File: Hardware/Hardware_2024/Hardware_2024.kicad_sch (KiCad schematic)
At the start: 53 parts, among them U1 Raspberry_Pi, U2 SHHD003A0A, U3 MCP3008

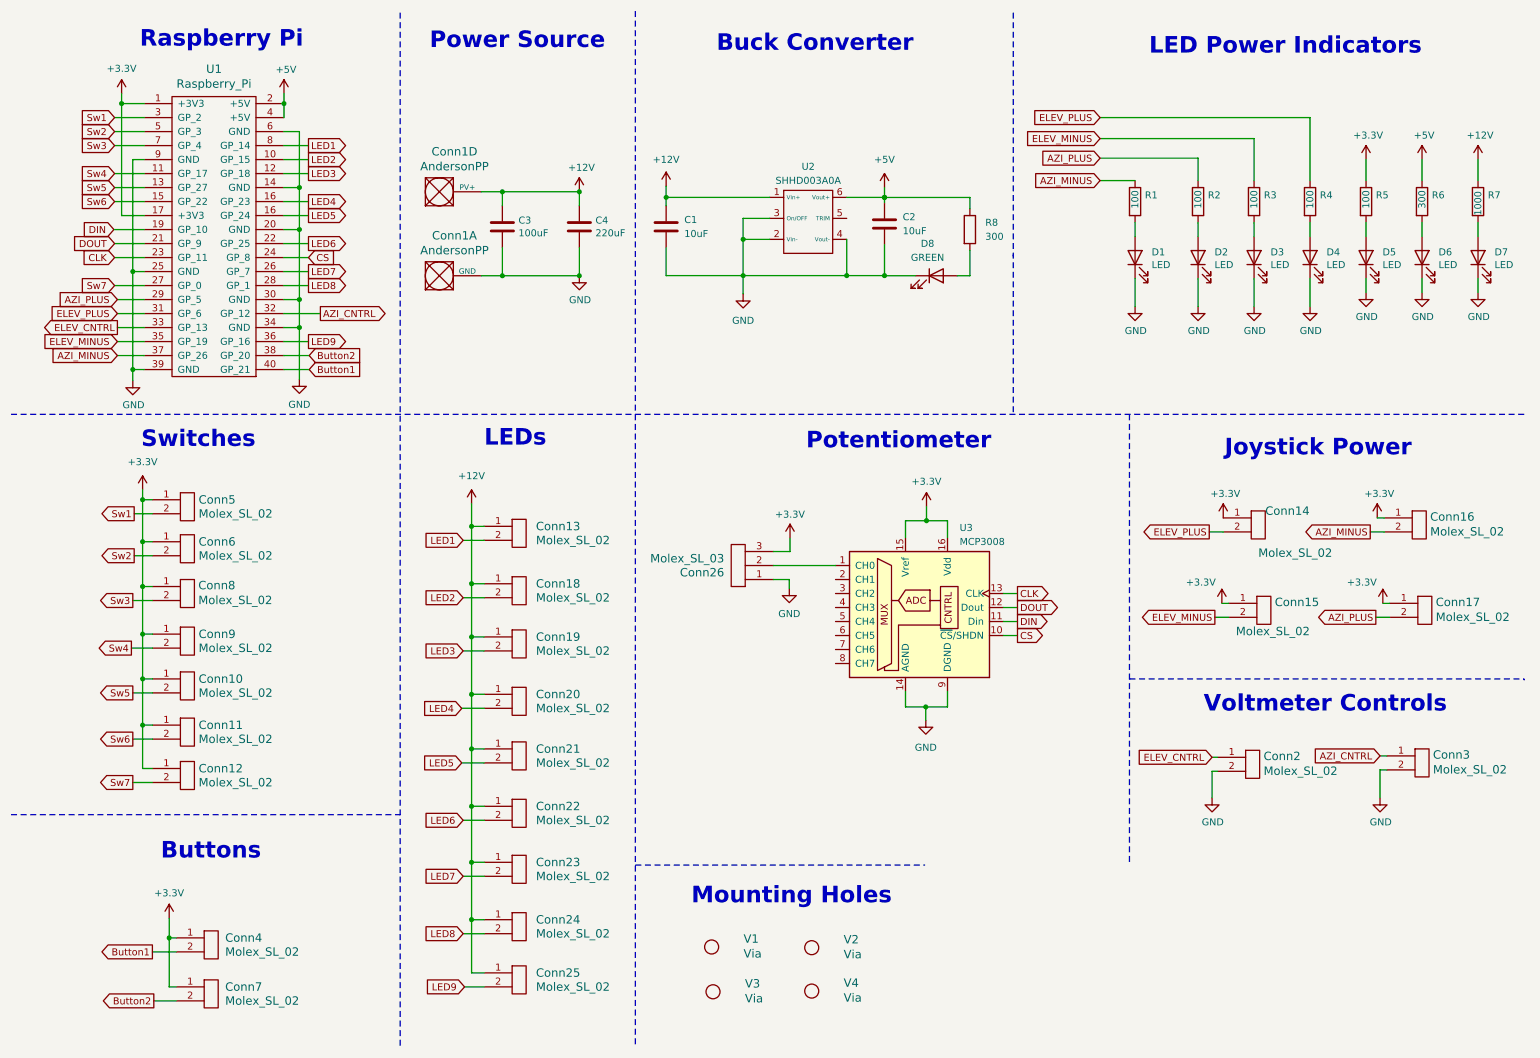
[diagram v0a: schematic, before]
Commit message: assigned footprints worked on layout
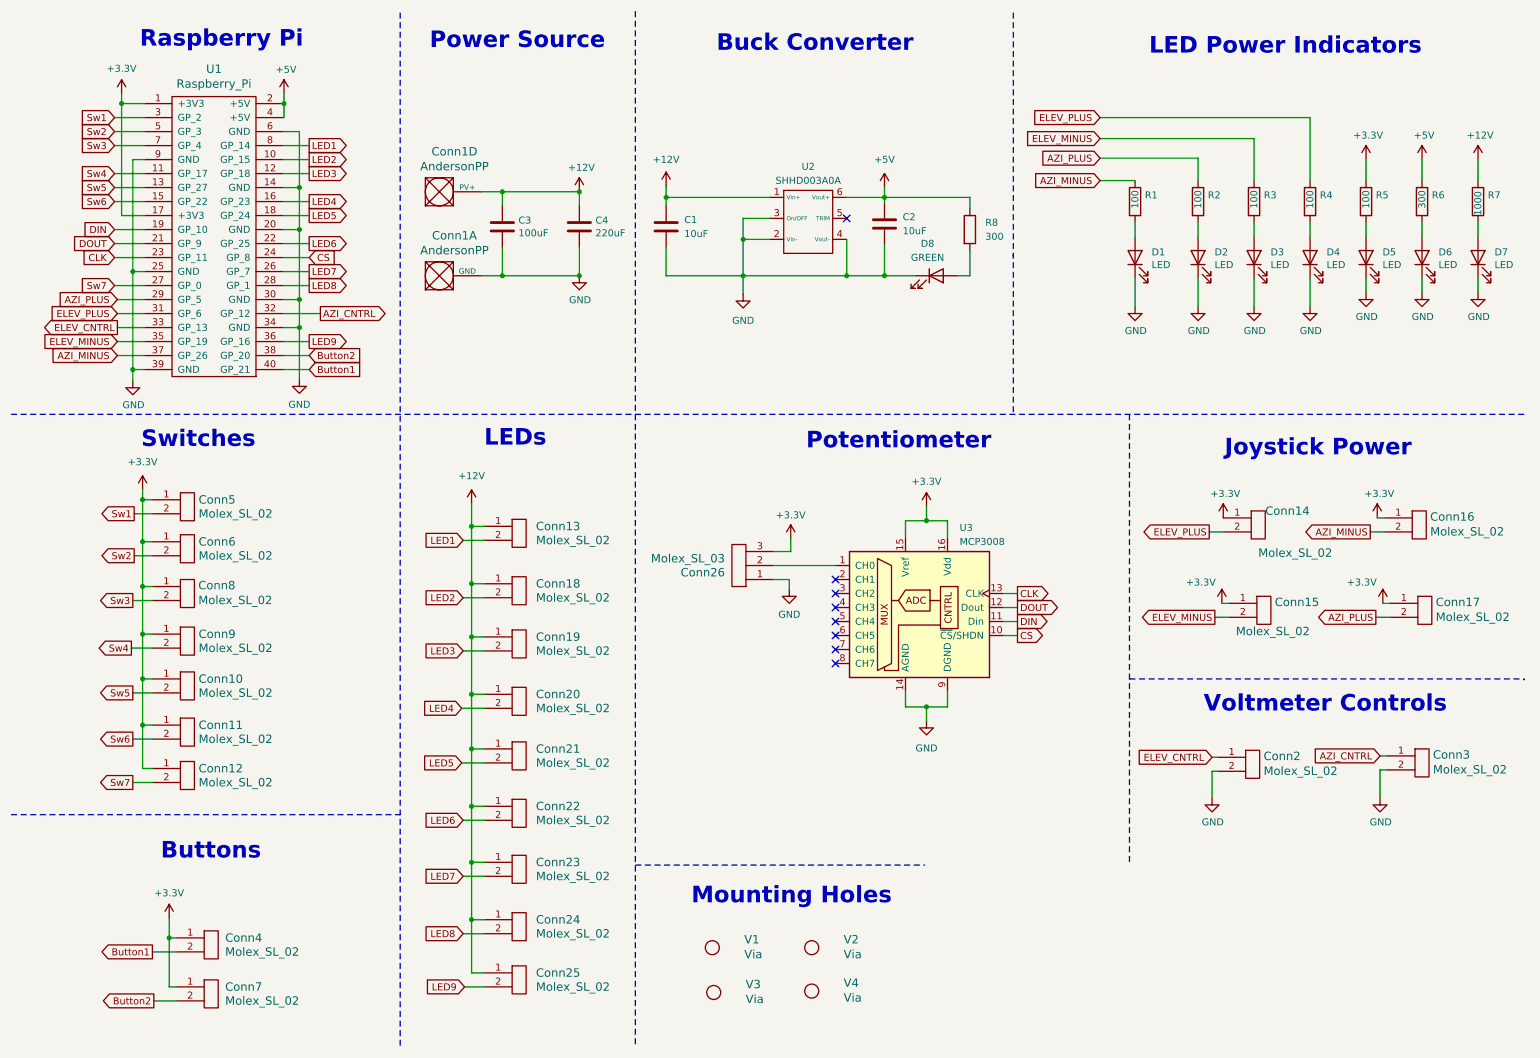
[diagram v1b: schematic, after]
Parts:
- C1, C2: footprint (none) -> Capacitor_SMD:C_0603_1608Metric
- Conn10, Conn11, Conn12, Conn13, Conn18, Conn19, Conn20, Conn21, Conn22, Conn23, Conn24, Conn25, Conn4, Conn5, Conn6, Conn7, Conn9: footprint (none) -> MRDT_Connectors:MOLEX_SL_02_Vertical
- Conn14, Conn16, Conn2, Conn3: footprint MRDT_Connectors:MOLEX_SL_02_Horizontal -> MRDT_Connectors:MOLEX_SL_02_Vertical
- Conn26: footprint (none) -> MRDT_Connectors:MOLEX_SL_03_Horizontal
- D8: footprint (none) -> LED_SMD:LED_0603_1608Metric_Pad1.05x0.95mm_HandSolder
- R8: footprint (none) -> Resistor_SMD:R_0603_1608Metric_Pad0.98x0.95mm_HandSolder
- U2: footprint MRDT_Devices:SHHD003A0A-SRZ -> SHHD003A04A41:SHHD003A0A-SRZ
- U3: footprint (none) -> Package_DIP:DIP-16_W7.62mm
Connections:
- net LED5: now also U1.18 (GP_24); no longer U1.16 (GP_24)
- no-connect marks 0 -> 8

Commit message: finished organizing. traces need work
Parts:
- removed D8: GREEN, LED_SMD:LED_0603_1608Metric_Pad1.05x0.95mm_HandSolder, symbol Device:LED
- removed R8: 300, Resistor_SMD:R_0603_1608Metric_Pad0.98x0.95mm_HandSolder, symbol Device:R
- Conn26: footprint MRDT_Connectors:MOLEX_SL_03_Horizontal -> MRDT_Connectors:MOLEX_SL_03_Vertical
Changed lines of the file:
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@@
   (junction (at 39.878 179.324) (diameter 0) (color 0 0 0 0)
-  )
-  (junction (at 169.672 59.182) (diameter 0) (color 0 0 0 0)
   )
   (junction (at 100.33 43.942) (diameter 0) (color 0 0 0 0)
@@
     (stroke (width 0) (type default))
   )
-  (wire (pts (xy 185.166 44.958) (xy 169.672 44.958))
-    (stroke (width 0) (type default))
-  )
   (wire (pts (xy 94.742 155.448) (xy 94.742 145.034))
     (stroke (width 0) (type default))
@@
     (stroke (width 0) (type default))
   )
-  (wire (pts (xy 185.166 54.61) (xy 185.166 59.182))
-    (stroke (width 0) (type default))
-  )
   (wire (pts (xy 94.742 135.128) (xy 97.028 135.128))
     (stroke (width 0) (type default))
@@
     (stroke (width 0) (type default))
   )
-  (wire (pts (xy 185.166 46.99) (xy 185.166 44.958))
-    (stroke (width 0) (type default))
-  )
   (wire (pts (xy 93.218 117.602) (xy 97.028 117.602))
     (stroke (width 0) (type default))
@@
     (stroke (width 0) (type default))
   )
-  (wire (pts (xy 175.26 59.182) (xy 169.672 59.182))
-    (stroke (width 0) (type default))
-  )
   (wire (pts (xy 60.706 40.64) (xy 65.278 40.64))
     (stroke (width 0) (type default))
@@
   (polyline (pts (xy 193.04 55.626) (xy 193.04 55.372))
     (stroke (width 0) (type dash))
-  )
-  (wire (pts (xy 185.166 59.182) (xy 182.88 59.182))
-    (stroke (width 0) (type default))
   )
   (wire (pts (xy 226.568 64.77) (xy 226.568 59.69))
@@
     )
     (property "Value" "10uF" (at 172.974 51.054 0)
-      (effects (font (size 1.27 1.27)) (justify left))
+      (effects (font (size 1.27 1.27)) (justify left) hide)
     )
     (property "Footprint" "Capacitor_SMD:C_0603_1608Metric" (at 170.6372 53.594 0)
@@
     )
   )
-  (symbol (lib_id "Device:R") (at 185.166 50.8 0) (unit 1)
-    (in_bom yes) (on_board yes) (dnp no) (fields_autoplaced)
-    (property "Reference" "R8" (at 187.96 49.53 0)
-      (effects (font (size 1.27 1.27)) (justify left))
-    )
-    (property "Value" "300" (at 187.96 52.07 0)
-      (effects (font (size 1.27 1.27)) (justify left))
-    )
-    (property "Footprint" "Resistor_SMD:R_0603_1608Metric_Pad0.98x0.95mm_HandSolder" (at 183.388 50.8 90)
-      (effects (font (size 1.27 1.27)) hide)
-    )
-    (property "Datasheet" "~" (at 185.166 50.8 0)
-      (effects (font (size 1.27 1.27)) hide)
-    )
-    (pin "1")
-    (pin "2")
-    (instances
-      (project "Hardware_2024"
-        (path "/925b1423-756e-4600-b210-badb8d52bba3"
-          (reference "R8") (unit 1)
-        )
-      )
-    )
-  )
   (symbol (lib_id "power:+3.3V") (at 152.654 106.934 0) (unit 1)
     (in_bom yes) (on_board yes) (dnp no)
@@
         (path "/925b1423-756e-4600-b210-badb8d52bba3"
           (reference "#PWR013") (unit 1)
-        )
-      )
-    )
-  )
-  (symbol (lib_id "Device:LED") (at 179.07 59.182 0) (unit 1)
-    (in_bom yes) (on_board yes) (dnp no) (fields_autoplaced)
-    (property "Reference" "D8" (at 177.4825 53.34 0)
-      (effects (font (size 1.27 1.27)))
-    )
-    (property "Value" "GREEN" (at 177.4825 55.88 0)
-      (effects (font (size 1.27 1.27)))
-    )
-    (property "Footprint" "LED_SMD:LED_0603_1608Metric_Pad1.05x0.95mm_HandSolder" (at 179.07 59.182 0)
-      (effects (font (size 1.27 1.27)) hide)
-    )
-    (property "Datasheet" "~" (at 179.07 59.182 0)
-      (effects (font (size 1.27 1.27)) hide)
-    )
-    (pin "1")
-    (pin "2")
-    (instances
-      (project "Hardware_2024"
-        (path "/925b1423-756e-4600-b210-badb8d52bba3"
-          (reference "D8") (unit 1)
         )
       )
@@
       (effects (font (size 1.524 1.524)) (justify left))
     )
-    (property "Footprint" "MRDT_Connectors:MOLEX_SL_03_Horizontal" (at 144.526 107.95 0)
-      (effects (font (size 1.524 1.524)) hide)
-    )
+    (property "Footprint" "MRDT_Connectors:MOLEX_SL_03_Vertical" (at 144.526 107.95 0)
+      (effects (font (size 1.524 1.524)) hide)
+    )

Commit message: Updated with changes
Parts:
- removed C3: 100uF, Capacitor_THT:CP_Radial_D6.3mm_P2.50mm, symbol Device:C
- removed C4: 220uF, Capacitor_THT:CP_Radial_D6.3mm_P2.50mm, symbol Device:C
- removed Conn10, Conn11, Conn12, Conn13, Conn18, Conn19, Conn20, Conn21, Conn22, Conn23, Conn24, Conn25, Conn4, Conn5, Conn6, Conn7, Conn8, Conn9: Molex_SL_02, MRDT_Connectors:MOLEX_SL_02_Vertical, symbol MRDT_Connectors:Molex_SL_02
- removed Conn26: Molex_SL_03, MRDT_Connectors:MOLEX_SL_03_Vertical, symbol MRDT_Connectors:Molex_SL_03
- removed D1, D2, D3, D4: LED, LED_SMD:LED_0603_1608Metric_Pad1.05x0.95mm_HandSolder, symbol Device:LED
- removed R1, R2, R3, R4: 100, Resistor_SMD:R_0603_1608Metric_Pad0.98x0.95mm_HandSolder, symbol Device:R
- removed U3: MCP3008, Package_DIP:DIP-16_W7.62mm, symbol Analog_ADC:MCP3008
- Conn1: footprint MRDT_Connectors:Square_Anderson_2_H_Stacked -> MRDT_Connectors:Square_Anderson_2_H_Side_By_Side
- U1: footprint MRDT_Shields:RASPBERRY_PI_HEADERS -> MRDT_Shields:RaspberryPi_THT_BOTTOM
- U2: footprint SHHD003A04A41:SHHD003A0A-SRZ -> MRDT_Devices:SHHD003A0A41Z_Through_Hole
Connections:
- net +3.3V is gone; now on net +3V3: U1.1 (+3V3), U1.17 (+3V3)
- net +12V: now also Conn1.2 (V+Log); no longer Conn1.4 (PV+)
- net Button1: no longer names the net of U1.40 (GP_21)
- net Button2: no longer names the net of U1.38 (GP_20)
- net CLK: no longer names the net of U1.23 (GP_11)
- net CS: no longer names the net of U1.24 (GP_8)
- net DIN: no longer names the net of U1.19 (GP_10)
- net DOUT: no longer names the net of U1.21 (GP_9)
- net LED1: no longer names the net of U1.8 (GP_14)
- net LED2: no longer names the net of U1.10 (GP_15)
- net LED3: no longer names the net of U1.12 (GP_18)
- net LED4: no longer names the net of U1.16 (GP_23)
- net LED5: no longer names the net of U1.18 (GP_24)
- net LED6: no longer names the net of U1.22 (GP_25)
- net LED7: no longer names the net of U1.26 (GP_7)
- net LED8: no longer names the net of U1.28 (GP_1)
- net LED9: no longer names the net of U1.36 (GP_16)
- net Sw1: no longer names the net of U1.3 (GP_2)
- net Sw2: no longer names the net of U1.5 (GP_3)
- net Sw3: no longer names the net of U1.7 (GP_4)
- net Sw4: no longer names the net of U1.11 (GP_17)
- net Sw5: no longer names the net of U1.13 (GP_27)
- net Sw6: no longer names the net of U1.15 (GP_22)
- net Sw7: no longer names the net of U1.27 (GP_0)
- no-connect marks 8 -> 23
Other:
- note removed: "Buttons"
- note removed: "LEDs"
- note removed: "Potentiometer"
- note removed: "Switches"
- moved on the sheet: C1, C2, Conn14, Conn15, Conn16, Conn17, Conn2, Conn3, D5, D6, D7, R5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
